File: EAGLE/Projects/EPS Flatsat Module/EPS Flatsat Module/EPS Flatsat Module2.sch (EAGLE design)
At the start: 32 parts, among them J1 ESQ-126-39-G-D, J2 ESQ-126-39-G-D, J3 TSW-110-23-F-D, J4 TSW-110-23-F-D, T1 2N3904, T2 2N3904, U1 Value, U2 Value, U3 Value, U4 Value, U5 Value, U6 Value

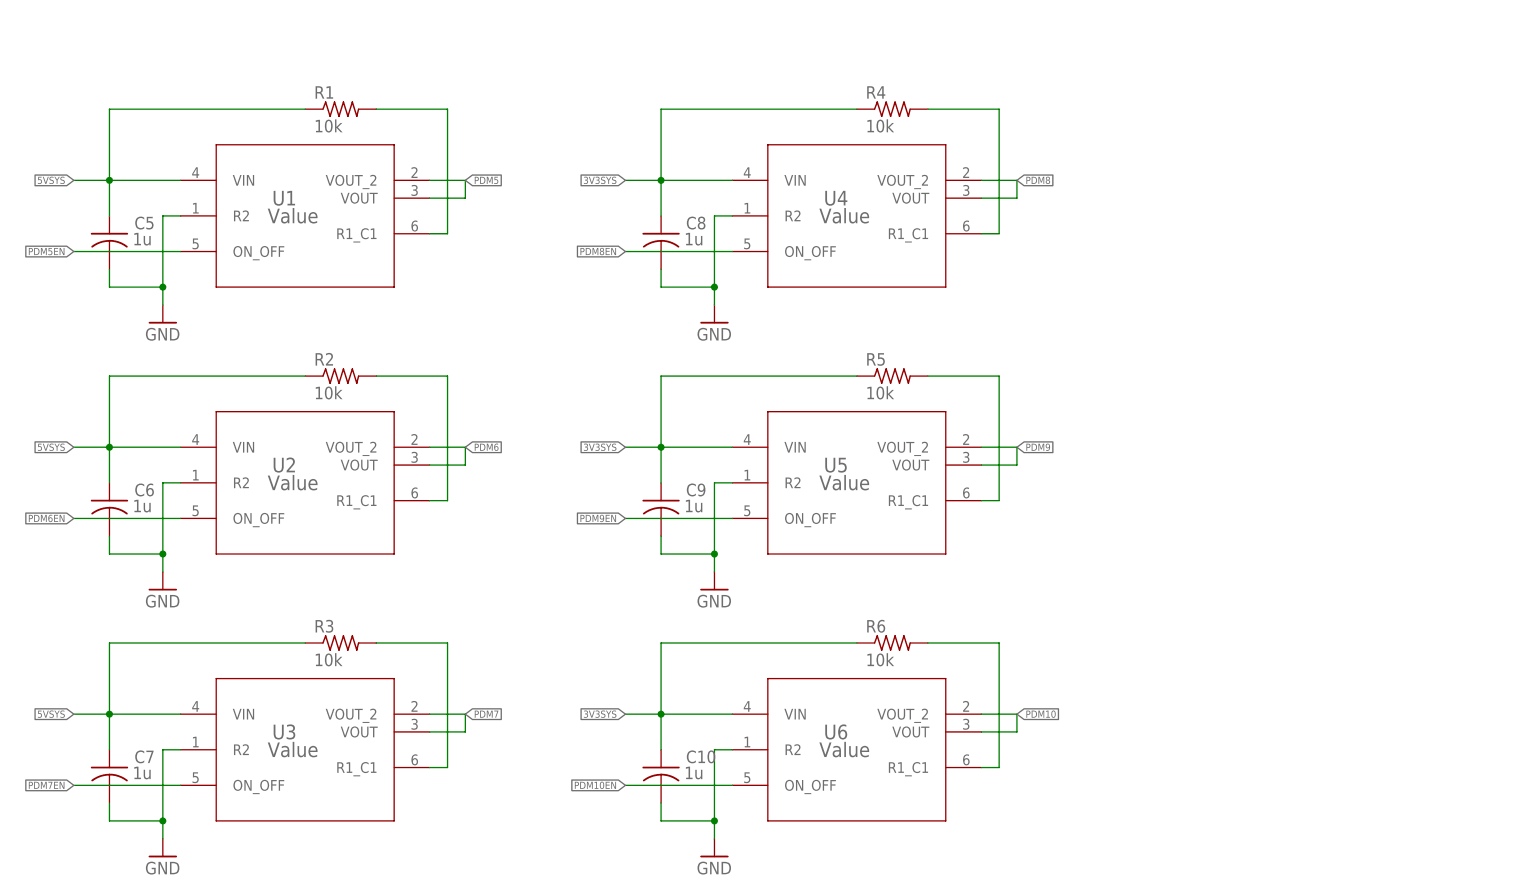
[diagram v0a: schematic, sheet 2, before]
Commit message: Updated flatsat module schematic/board
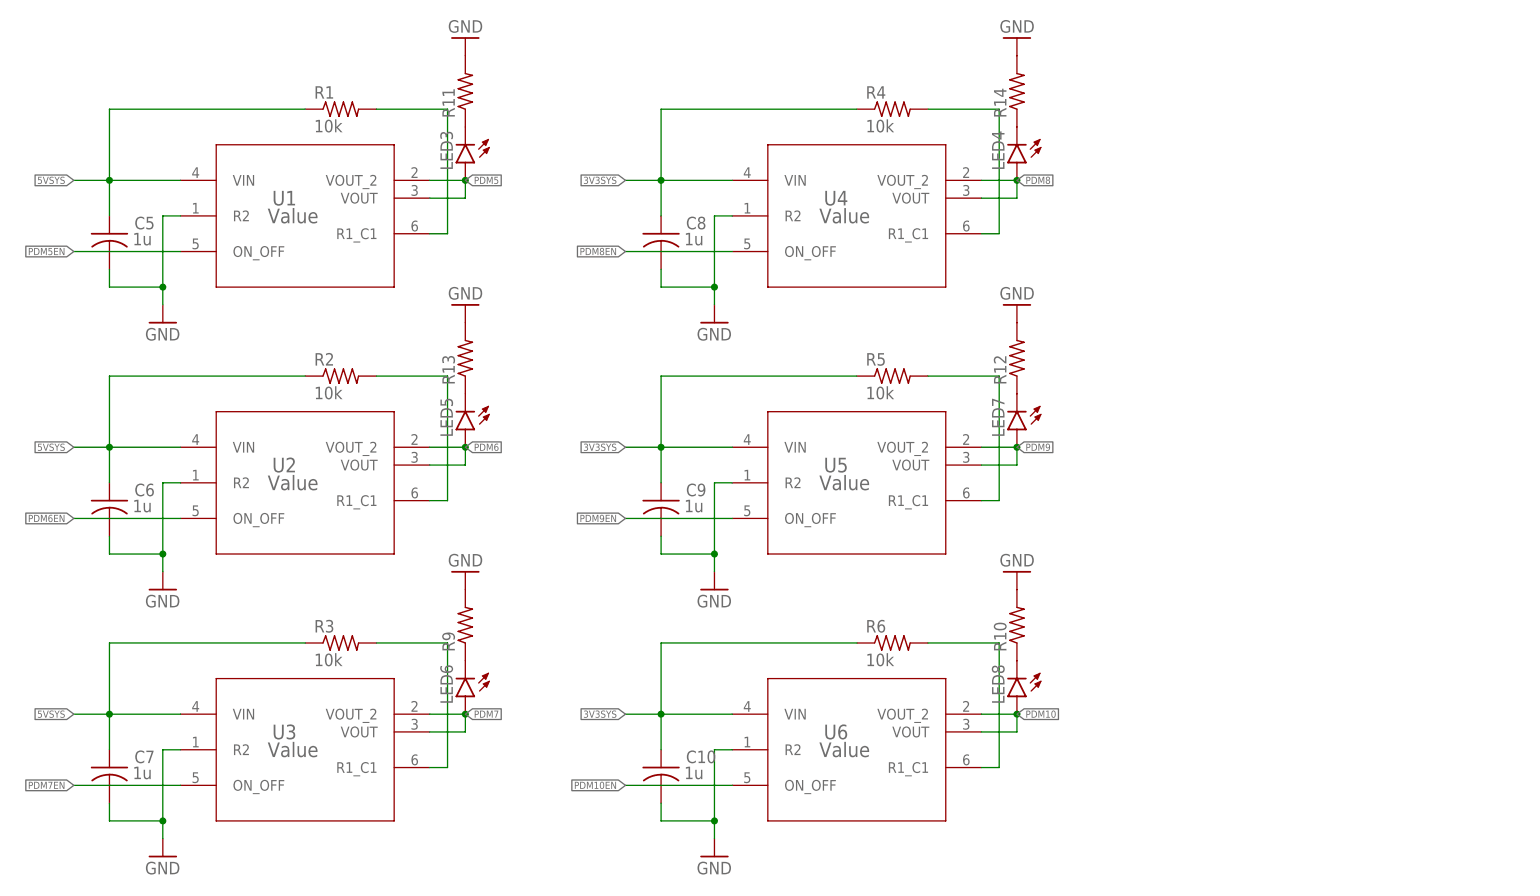
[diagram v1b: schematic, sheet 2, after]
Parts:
- added F1: (no value), fuse:19559
- added J5: 1985881, 1985881:1985881
- added LED1, LED2, LED3, LED4, LED5, LED6, LED7, LED8: (no value), led:LEDCHIPLED_0805
- added R10, R11, R12, R13, R14, R7, R8, R9: (no value), rcl:R-US_R0805
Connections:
- new net N$10: LED2.C, R7.1
- new net N$11: LED6.C, R9.1
- new net N$12: LED3.C, R11.1
- new net N$13: LED4.C, R14.1
- new net N$14: LED7.C, R12.1
- new net N$15: LED5.C, R13.1
- new net N$16: LED8.C, R10.1
- new net N$17: F1.2, J5.1
- new net N$9: LED1.C, R8.1
- net 3V3SYS: now also LED2.A
- net 5VSYS: now also LED1.A
- net GND: now also J5.2, R10.2, R11.2, R12.2, R13.2, R14.2, R7.2, R8.2, R9.2
- net PDM10: now also LED8.A
- net PDM5: now also LED3.A
- net PDM6: now also LED5.A
- net PDM7: now also LED6.A
- net PDM8: now also LED4.A
- net PDM9: now also LED7.A
- net VIN: now also F1.1

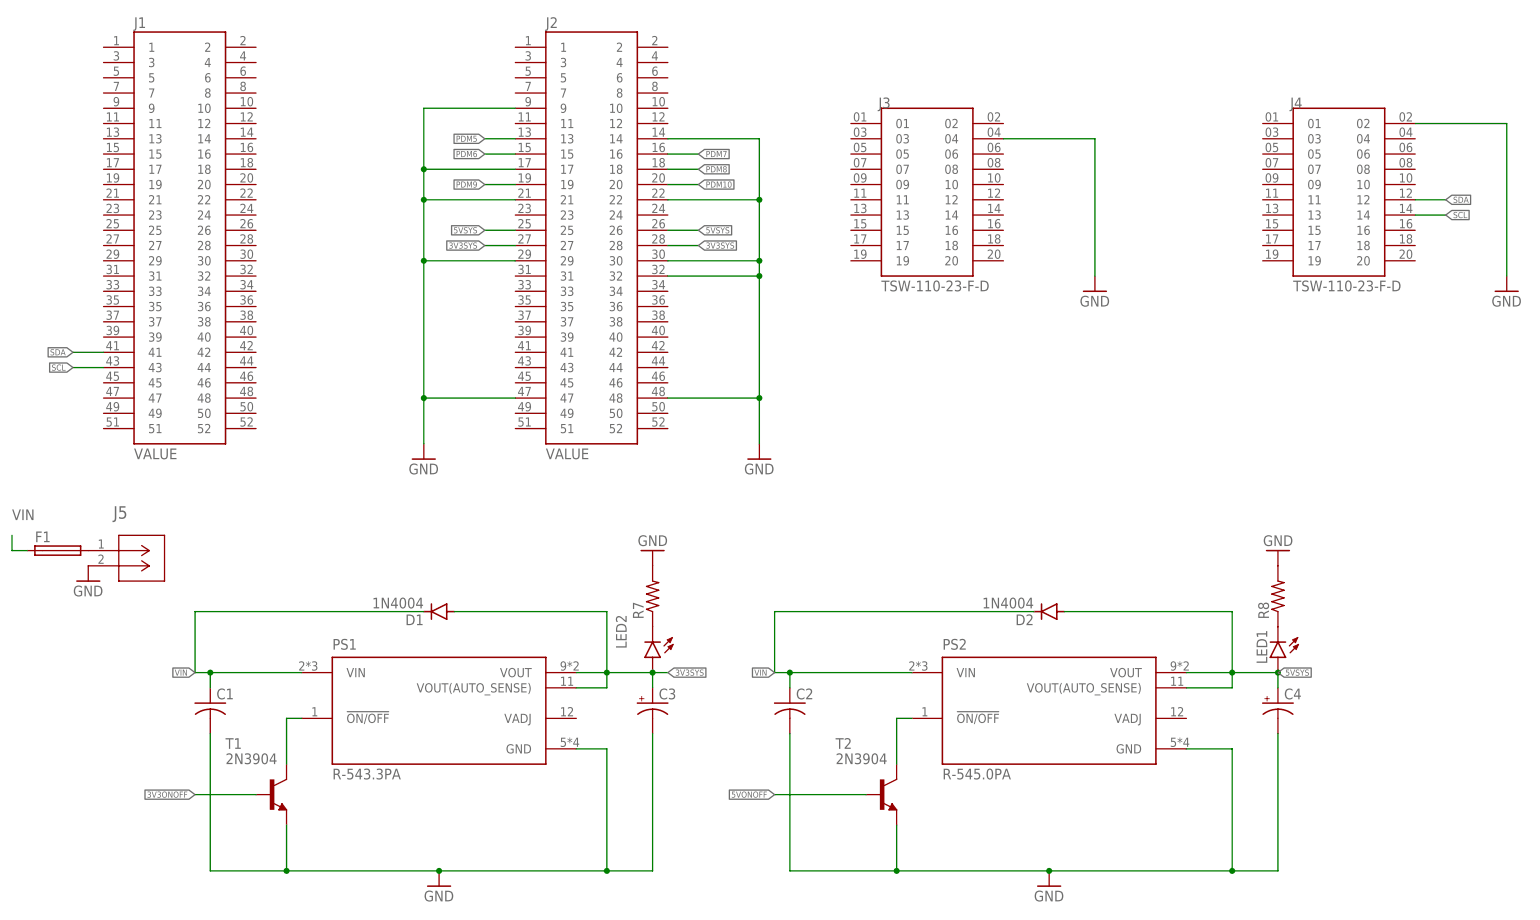
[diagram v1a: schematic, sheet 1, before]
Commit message: Updated fuse, changed MSP header spacing, small layout edits
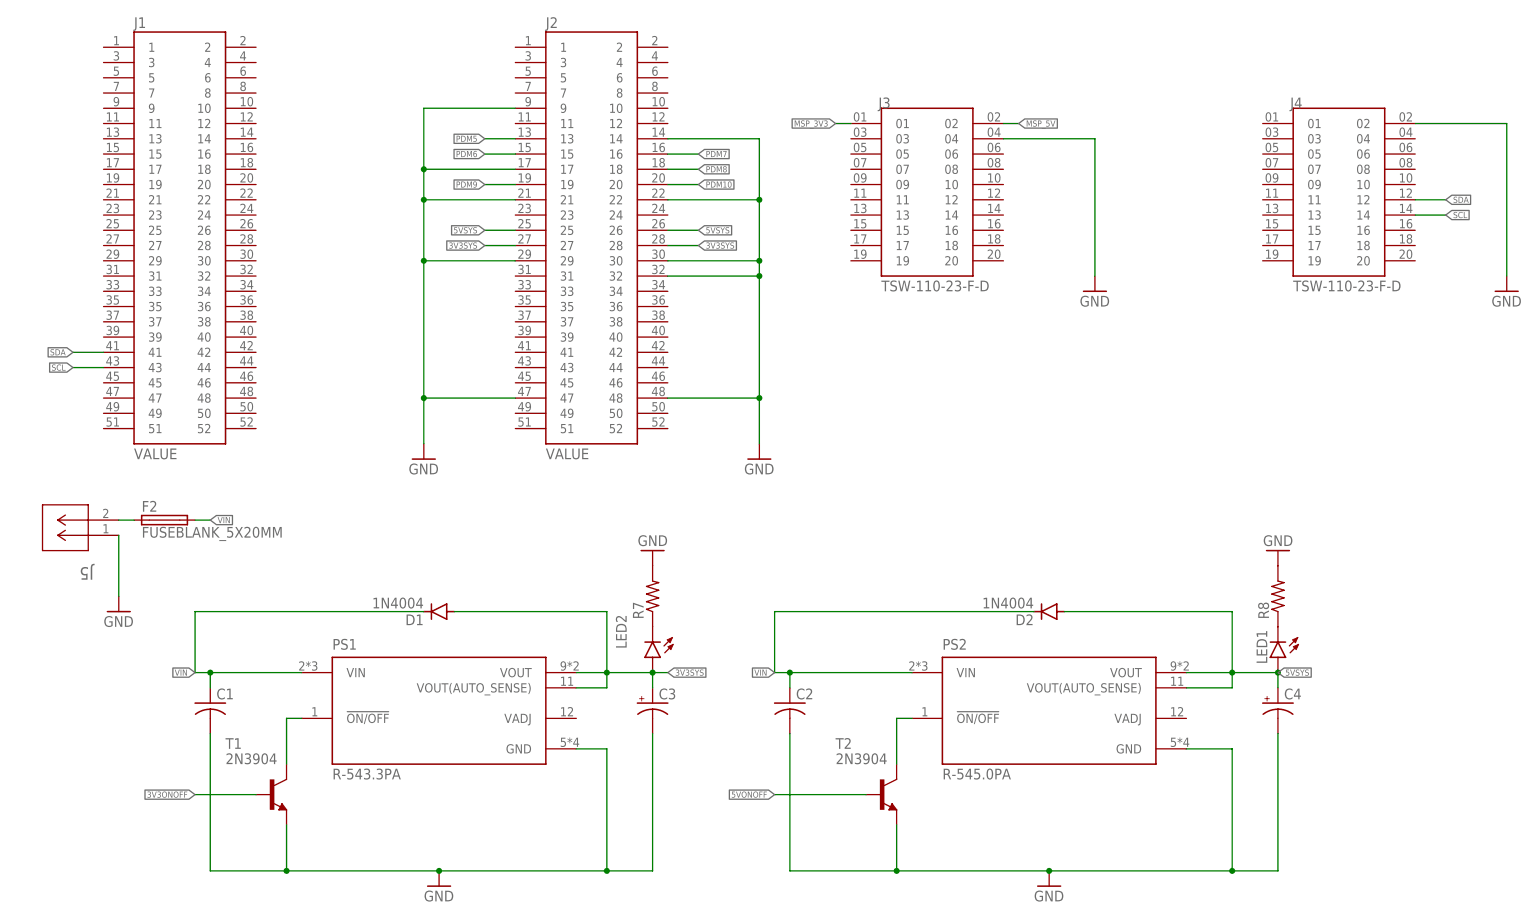
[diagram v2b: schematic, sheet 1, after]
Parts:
- removed F1: (no value), fuse:19559
- added F2: FUSEBLANK_5X20MM, fuse:FUSEBLANK_5X20MM
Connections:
- new net MSP_3V3: J3.01
- new net MSP_5V: J3.02
- net GND: now also J5.1; no longer J5.2
- net N$17: now also F2.1, J5.2; no longer F1.2, J5.1
- net VIN: now also F2.2; no longer F1.1
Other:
- moved on the sheet: J5
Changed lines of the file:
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@@
 <?xml version="1.0" encoding="utf-8"?>
 <!DOCTYPE eagle SYSTEM "eagle.dtd">
-<eagle version="9.6.2">
+<eagle version="9.5.1">
 <drawing>
 <settings>
@@
 <classes>
 <class number="0" name="default" width="0" drill="0">
+</class>
+<class number="1" name="power" width="0.2032" drill="0">
 </class>
 </classes>
@@
 <part name="GND20" library="supply1" library_urn="urn:adsk.eagle:library:371" deviceset="GND" device=""/>
 <part name="GND21" library="supply1" library_urn="urn:adsk.eagle:library:371" deviceset="GND" device=""/>
-<part name="F1" library="fuse" library_urn="urn:adsk.eagle:library:233" deviceset="19559" device="" package3d_urn="urn:adsk.eagle:package:14056/1"/>
+<part name="F2" library="fuse" library_urn="urn:adsk.eagle:library:233" deviceset="FUSE" device="BLANK_5X20MM" package3d_urn="urn:adsk.eagle:package:14079/1"/>
 </parts>
 <sheets>
@@
 <attribute name="VALUE" x="216.916" y="87.249" size="1.778" layer="96"/>
 </instance>
-<instance part="J5" gate="A" x="17.78" y="116.84" smashed="yes">
-<attribute name="NAME" x="21.9456" y="122.1486" size="2.0828" layer="95" ratio="6" rot="SR0"/>
-</instance>
-<instance part="GND13" gate="1" x="17.78" y="111.76" smashed="yes">
-<attribute name="VALUE" x="15.24" y="109.22" size="1.778" layer="96"/>
+<instance part="J5" gate="A" x="22.86" y="119.38" smashed="yes" rot="R180">
+<attribute name="NAME" x="18.6944" y="114.0714" size="2.0828" layer="95" ratio="6" rot="SR180"/>
+</instance>
+<instance part="GND13" gate="1" x="22.86" y="106.68" smashed="yes">
+<attribute name="VALUE" x="20.32" y="104.14" size="1.778" layer="96"/>
 </instance>
 <instance part="LED1" gate="G$1" x="215.9" y="99.06" smashed="yes" rot="R180">
@@
 <attribute name="VALUE" x="218.44" y="119.38" size="1.778" layer="96" rot="R180"/>
 </instance>
-<instance part="F1" gate="1" x="12.7" y="116.84" smashed="yes">
-<attribute name="NAME" x="8.89" y="118.237" size="1.778" layer="95"/>
-<attribute name="VALUE" x="8.89" y="113.919" size="1.778" layer="96"/>
+<instance part="F2" gate="G$1" x="30.48" y="121.92" smashed="yes">
+<attribute name="NAME" x="26.67" y="123.317" size="1.778" layer="95"/>
+<attribute name="VALUE" x="26.67" y="118.999" size="1.778" layer="96"/>
 </instance>
 </instances>
@@
 </segment>
 </net>
-<net name="5VSYS" class="0">
+<net name="5VSYS" class="1">
 <segment>
 <pinref part="J2" gate="G$1" pin="25"/>
@@
 </segment>
 </net>
-<net name="GND" class="0">
+<net name="GND" class="1">
 <segment>
 <pinref part="GND1" gate="1" pin="GND"/>
@@
 <segment>
 <pinref part="GND13" gate="1" pin="GND"/>
-<pinref part="J5" gate="A" pin="2"/>
+<pinref part="J5" gate="A" pin="1"/>
+<wire x1="22.86" y1="119.38" x2="22.86" y2="109.22" width="0.1524" layer="91"/>
 </segment>
 <segment>
@@
 </segment>
 </net>
-<net name="3V3SYS" class="0">
+<net name="3V3SYS" class="1">
 <segment>
 <pinref part="J2" gate="G$1" pin="27"/>
@@
 </segment>
 </net>
-<net name="PDM5" class="0">
+<net name="PDM5" class="1">
 <segment>
 <pinref part="J2" gate="G$1" pin="13"/>
@@
 </segment>
 </net>
-<net name="PDM6" class="0">
+<net name="PDM6" class="1">
 <segment>
 <pinref part="J2" gate="G$1" pin="15"/>
@@
 </segment>
 </net>
-<net name="PDM7" class="0">
+<net name="PDM7" class="1">
 <segment>
 <pinref part="J2" gate="G$1" pin="16"/>
@@
 </segment>
 </net>
-<net name="PDM8" class="0">
+<net name="PDM8" class="1">
 <segment>
 <pinref part="J2" gate="G$1" pin="18"/>
@@
 </segment>
 </net>
-<net name="PDM9" class="0">
+<net name="PDM9" class="1">
 <segment>
 <pinref part="J2" gate="G$1" pin="19"/>
@@
 </segment>
 </net>
-<net name="PDM10" class="0">
+<net name="PDM10" class="1">
 <segment>
 <pinref part="J2" gate="G$1" pin="20"/>
@@
 </segment>
 </net>
-<net name="VIN" class="0">
+<net name="VIN" class="1">
 <segment>
 <pinref part="PS1" gate="G$1" pin="VIN"/>
@@
 </segment>
 <segment>
-<pinref part="F1" gate="1" pin="1"/>
-<wire x1="7.62" y1="116.84" x2="5.08" y2="116.84" width="0.1524" layer="91"/>
-<wire x1="5.08" y1="116.84" x2="5.08" y2="119.38" width="0.1524" layer="91"/>
-<label x="5.08" y="121.92" size="1.778" layer="95"/>
+<pinref part="F2" gate="G$1" pin="2"/>
+<wire x1="35.56" y1="121.92" x2="38.1" y2="121.92" width="0.1524" layer="91"/>
+<label x="38.1" y="121.92" size="1.016" layer="95" xref="yes"/>
 </segment>
 </net>
@@
 </segment>
 </net>
-<net name="N$17" class="0">
-<segment>
-<pinref part="J5" gate="A" pin="1"/>
-<pinref part="F1" gate="1" pin="2"/>
+<net name="MSP_3V3" class="1">
+<segment>
+<pinref part="J3" gate="G$1" pin="01"/>
+<wire x1="144.78" y1="187.96" x2="142.24" y2="187.96" width="0.1524" layer="91"/>
+<label x="142.24" y="187.96" size="1.016" layer="95" rot="R180" xref="yes"/>
+</segment>
+</net>
+<net name="MSP_5V" class="1">
+<segment>
+<pinref part="J3" gate="G$1" pin="02"/>
+<wire x1="170.18" y1="187.96" x2="172.72" y2="187.96" width="0.1524" layer="91"/>
+<label x="172.72" y="187.96" size="1.016" layer="95" xref="yes"/>
+</segment>
+</net>
+<net name="N$17" class="1">
+<segment>
+<pinref part="J5" gate="A" pin="2"/>
+<pinref part="F2" gate="G$1" pin="1"/>
+<wire x1="22.86" y1="121.92" x2="25.4" y2="121.92" width="0.1524" layer="91"/>
 </segment>
 </net>
@@
 </segment>
 </net>
-<net name="GND" class="0">
+<net name="GND" class="1">
 <segment>
 <pinref part="U1" gate="A" pin="R2"/>
@@
 </segment>
 </net>
-<net name="5VSYS" class="0">
+<net name="5VSYS" class="1">
 <segment>
 <pinref part="U1" gate="A" pin="VIN"/>
@@
 </segment>
 </net>
-<net name="PDM5" class="0">
+<net name="PDM5" class="1">
 <segment>
 <pinref part="U1" gate="A" pin="VOUT_2"/>
@@
 </segment>
 </net>
-<net name="PDM6" class="0">
+<net name="PDM6" class="1">
 <segment>
 <pinref part="U2" gate="A" pin="VOUT_2"/>
@@
 </segment>
 </net>
-<net name="3V3SYS" class="0">
+<net name="3V3SYS" class="1">
 <segment>
 <pinref part="U4" gate="A" pin="VIN"/>
@@
 </segment>
 </net>
-<net name="PDM7" class="0">
+<net name="PDM7" class="1">
 <segment>
 <pinref part="U3" gate="A" pin="VOUT_2"/>
@@
 </segment>
 </net>
-<net name="PDM8" class="0">
+<net name="PDM8" class="1">
 <segment>
 <pinref part="U4" gate="A" pin="VOUT_2"/>
@@
 </segment>
 </net>
-<net name="PDM9" class="0">
+<net name="PDM9" class="1">
 <segment>
 <pinref part="U5" gate="A" pin="VOUT_2"/>
@@
 </segment>
 </net>
-<net name="PDM10" class="0">
+<net name="PDM10" class="1">
 <segment>
 <pinref part="U6" gate="A" pin="VOUT_2"/>

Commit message: Added TVS diode, changed microcontroller to Arduino Nano, redid traces
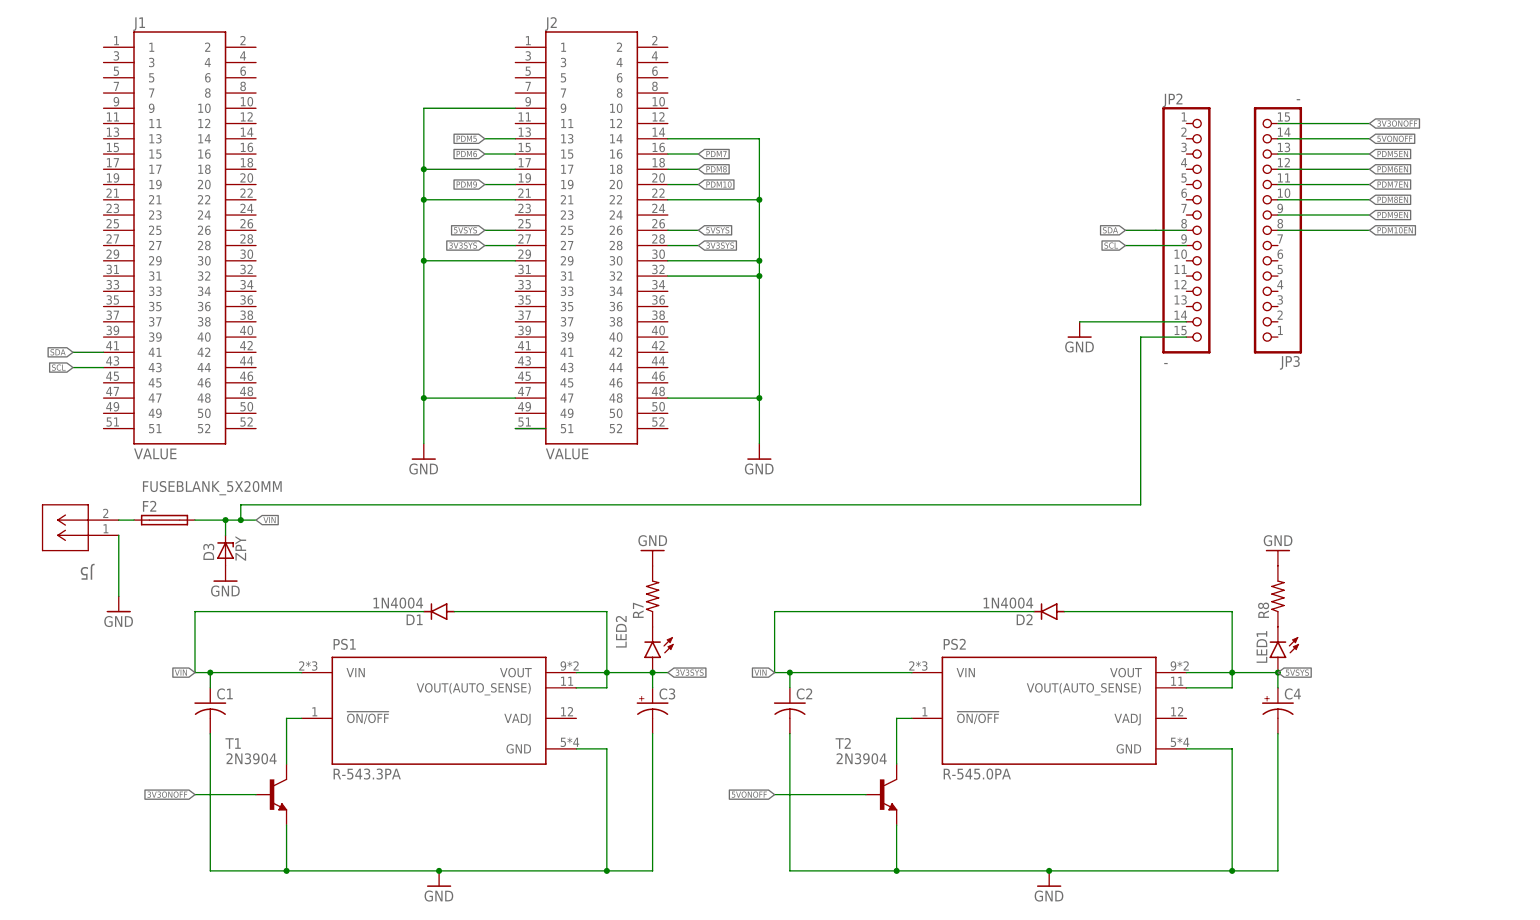
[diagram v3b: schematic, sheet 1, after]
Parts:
- removed J3, J4: TSW-110-23-F-D, TSW-110-23-F-D:TSW-110-23-F-D
- added D3: ZPY, diode:ZPY
- added JP2, JP3: -, Arduino-connectors:PINHD-1X15-CASTELLATED
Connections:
- removed net MSP_3V3: J3.01
- removed net MSP_5V: J3.02
- new net N$19: J2.51
- net 3V3ONOFF: now also JP3.15
- net 5VONOFF: now also JP3.14
- net GND: now also D3.A, JP2.14; no longer J3.04, J4.02
- net PDM10EN: now also JP3.8
- net PDM5EN: now also JP3.13
- net PDM6EN: now also JP3.12
- net PDM7EN: now also JP3.11
- net PDM8EN: now also JP3.10
- net PDM9EN: now also JP3.9
- net SCL: now also JP2.9; no longer J4.14
- net SDA: now also JP2.8; no longer J4.12
- net VIN: now also D3.C, JP2.15
